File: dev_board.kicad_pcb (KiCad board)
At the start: 2 copper layers, 52 x 71.5 mm, 49 parts, among them J1 USB_B_Micro, J2 Conn_02x26_Odd_Even, J3 Conn_02x26_Odd_Even, J4 SM03B-SRSS-TB, SW1 SW_Push, SW2 SW_Push, U1 RP2350_80QFN, U2 NCP1117-3.3_SOT223, U3 W25Q128JVS, U4 DNF, Y1 ABM8-272-T3

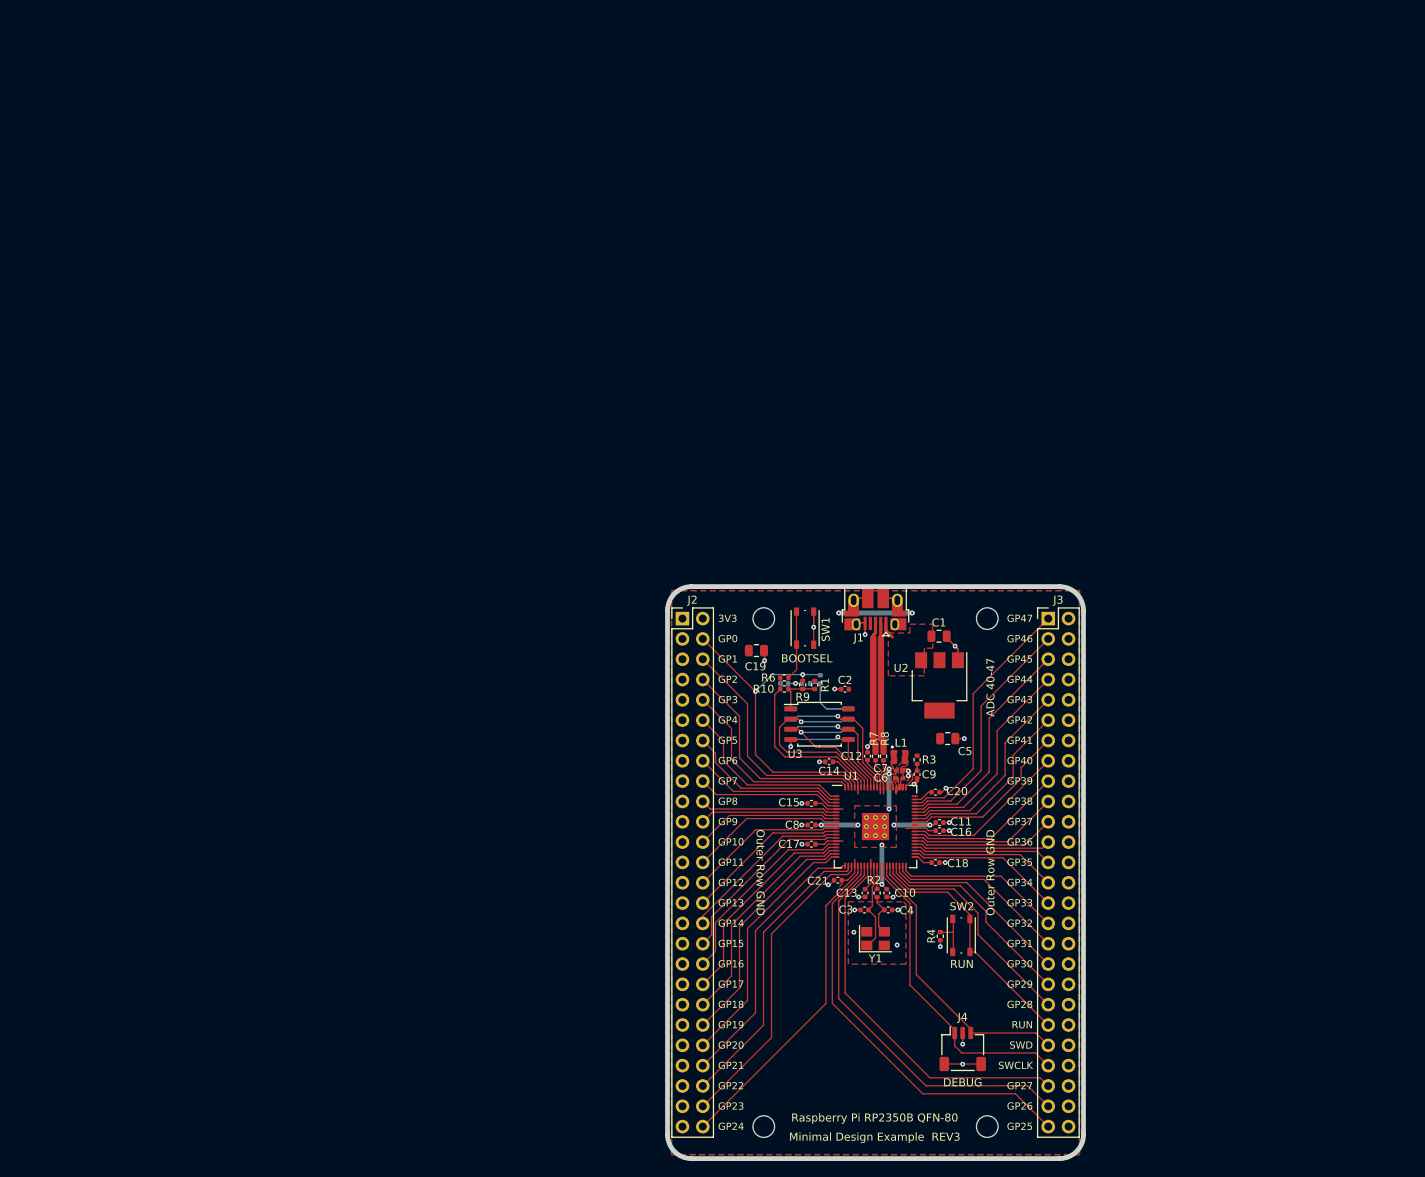
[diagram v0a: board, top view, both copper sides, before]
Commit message: more pcb chanegs, ADC fixes
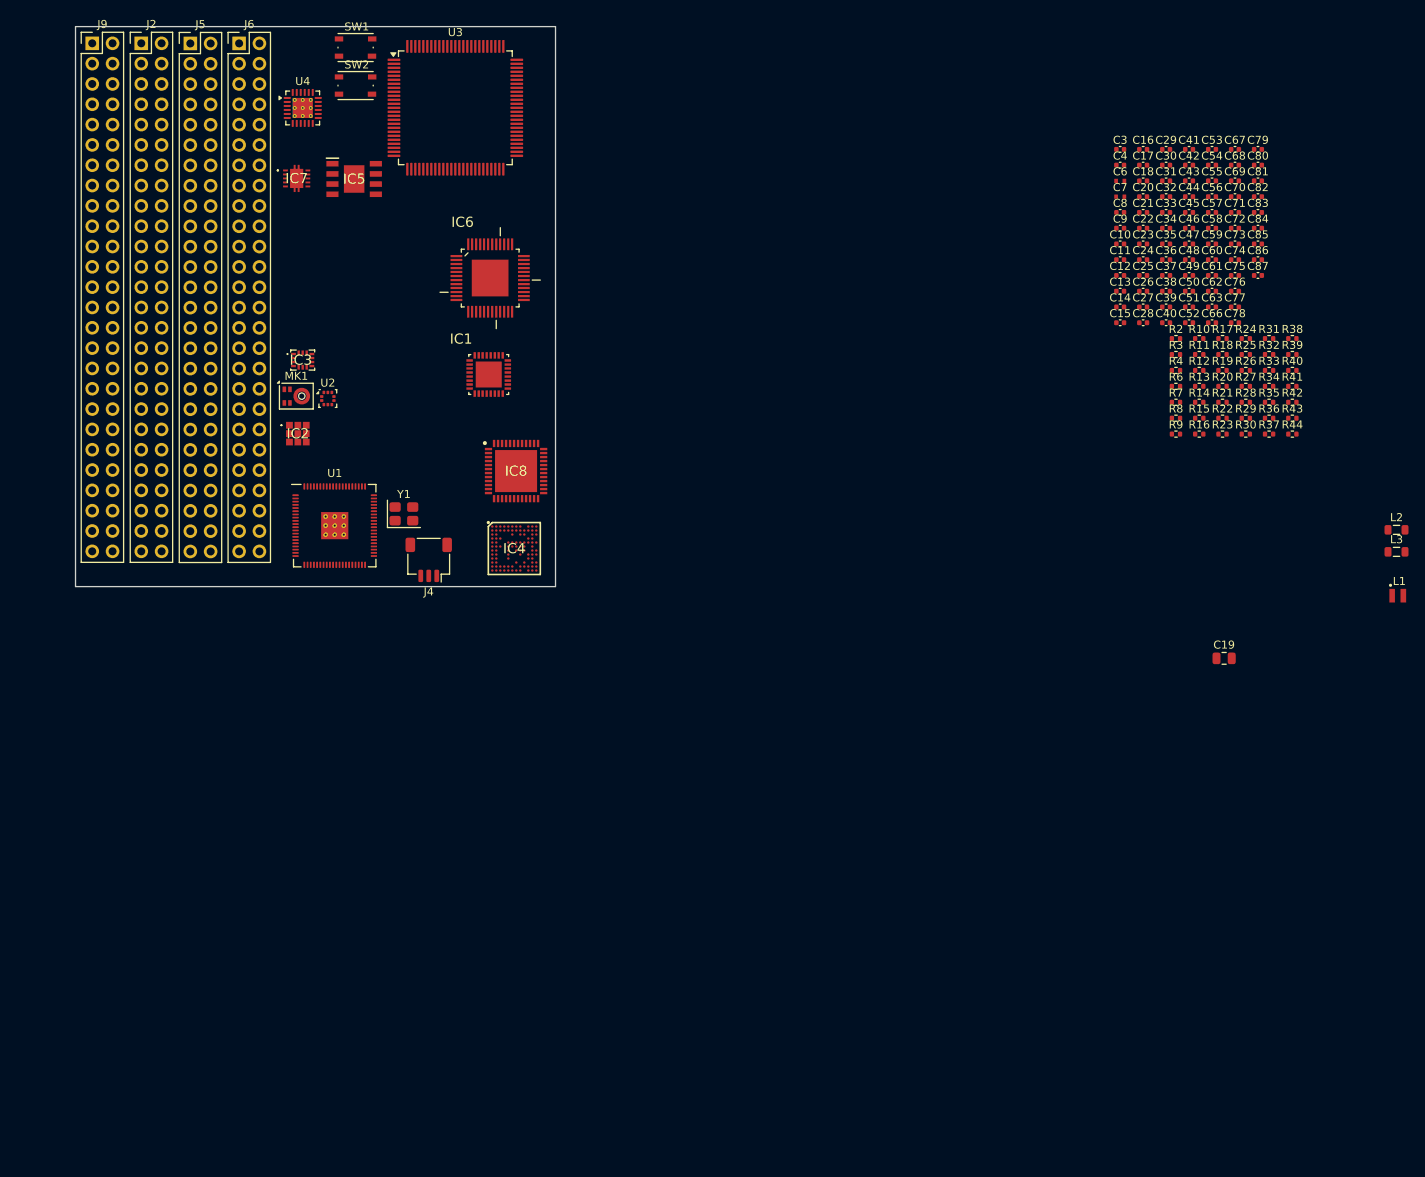
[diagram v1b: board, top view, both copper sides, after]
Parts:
- removed C1, C5: 10u, Capacitor_SMD:C_0805_2012Metric
- removed C2: 100n, Capacitor_SMD:C_0402_1005Metric
- removed H1, H2, H3, H4: MountingHole, MountingHole:MountingHole_2.7mm_M2.5
- removed J1: USB_B_Micro, Connector_USB:USB_Micro-B_Amphenol_10103594-0001LF_Horizontal
- removed J3: Conn_02x26_Odd_Even, Connector_PinHeader_2.54mm:PinHeader_2x26_P2.54mm_Vertical
- removed R1: DNF, Resistor_SMD:R_0402_1005Metric
- added C23: 100n, Capacitor_SMD:C_0402_1005Metric, F.Cu at (133.5, 27.2)
- added C24: 100n, Capacitor_SMD:C_0402_1005Metric, F.Cu at (133.5, 29.1)
- added C25: 10u, Capacitor_SMD:C_0402_1005Metric, F.Cu at (133.5, 31.1)
- added C26: 100n, Capacitor_SMD:C_0402_1005Metric, F.Cu at (133.5, 33.1)
- added C27: 100n, Capacitor_SMD:C_0402_1005Metric, F.Cu at (133.5, 35.0)
- added C28: 10u, Capacitor_SMD:C_0402_1005Metric, F.Cu at (133.5, 37.0)
- added C29: 1u, Capacitor_SMD:C_0402_1005Metric, F.Cu at (136.3, 15.3)
- added C30: 10u, Capacitor_SMD:C_0402_1005Metric, F.Cu at (136.3, 17.3)
- added C31: 10u, Capacitor_SMD:C_0402_1005Metric, F.Cu at (136.3, 19.3)
- added C32: 1u, Capacitor_SMD:C_0402_1005Metric, F.Cu at (136.3, 21.3)
- added C33: 100n, Capacitor_SMD:C_0402_1005Metric, F.Cu at (136.3, 23.2)
- added C34: 10u, Capacitor_SMD:C_0402_1005Metric, F.Cu at (136.3, 25.2)
- added C35: 10u, Capacitor_SMD:C_0402_1005Metric, F.Cu at (136.3, 27.2)
- added C36: 1u, Capacitor_SMD:C_0402_1005Metric, F.Cu at (136.3, 29.1)
- added C37: 1u, Capacitor_SMD:C_0402_1005Metric, F.Cu at (136.3, 31.1)
- added C38: 100n, Capacitor_SMD:C_0402_1005Metric, F.Cu at (136.3, 33.1)
- added C39: 10n, Capacitor_SMD:C_0402_1005Metric, F.Cu at (136.3, 35.0)
- added C40: 10n, Capacitor_SMD:C_0402_1005Metric, F.Cu at (136.3, 37.0)
- added C41: 100n, Capacitor_SMD:C_0402_1005Metric, F.Cu at (139.2, 15.3)
- added C42: 100n, Capacitor_SMD:C_0402_1005Metric, F.Cu at (139.2, 17.3)
- added C43: 100n, Capacitor_SMD:C_0402_1005Metric, F.Cu at (139.2, 19.3)
- added C44: 100n, Capacitor_SMD:C_0402_1005Metric, F.Cu at (139.2, 21.3)
- added C45: 100n, Capacitor_SMD:C_0402_1005Metric, F.Cu at (139.2, 23.2)
- added C46: 10u, Capacitor_SMD:C_0402_1005Metric, F.Cu at (139.2, 25.2)
- added C47: 2.2u, Capacitor_SMD:C_0402_1005Metric, F.Cu at (139.2, 27.2)
- added C48: 2.2u, Capacitor_SMD:C_0402_1005Metric, F.Cu at (139.2, 29.1)
- added C49: 100n, Capacitor_SMD:C_0402_1005Metric, F.Cu at (139.2, 31.1)
- added C50: 100n, Capacitor_SMD:C_0402_1005Metric, F.Cu at (139.2, 33.1)
- added C51: 100n, Capacitor_SMD:C_0402_1005Metric, F.Cu at (139.2, 35.0)
- added C52: 100n, Capacitor_SMD:C_0402_1005Metric, F.Cu at (139.2, 37.0)
- added C53: 10u, Capacitor_SMD:C_0402_1005Metric, F.Cu at (142.1, 15.3)
- added C54: 100n, Capacitor_SMD:C_0402_1005Metric, F.Cu at (142.1, 17.3)
- added C55: 100n, Capacitor_SMD:C_0402_1005Metric, F.Cu at (142.1, 19.3)
- added C56: 100n, Capacitor_SMD:C_0402_1005Metric, F.Cu at (142.1, 21.3)
- added C57: 100n, Capacitor_SMD:C_0402_1005Metric, F.Cu at (142.1, 23.2)
- added C58: 10u, Capacitor_SMD:C_0402_1005Metric, F.Cu at (142.1, 25.2)
- added C59: 100n, Capacitor_SMD:C_0402_1005Metric, F.Cu at (142.1, 27.2)
- added C60: 1u, Capacitor_SMD:C_0402_1005Metric, F.Cu at (142.1, 29.1)
- added C61: 100n, Capacitor_SMD:C_0402_1005Metric, F.Cu at (142.1, 31.1)
- added C62: 10u, Capacitor_SMD:C_0402_1005Metric, F.Cu at (142.1, 33.1)
- added C63: 100n, Capacitor_SMD:C_0402_1005Metric, F.Cu at (142.1, 35.0)
- added C66: 100n, Capacitor_SMD:C_0402_1005Metric, F.Cu at (142.1, 37.0)
- added C67: 100n, Capacitor_SMD:C_0402_1005Metric, F.Cu at (144.9, 15.3)
- added C68: 10u, Capacitor_SMD:C_0402_1005Metric, F.Cu at (144.9, 17.3)
- added C69: 2.2u, Capacitor_SMD:C_0402_1005Metric, F.Cu at (144.9, 19.3)
- added C70: 10u, Capacitor_SMD:C_0402_1005Metric, F.Cu at (144.9, 21.3)
- added C71: 2.2u, Capacitor_SMD:C_0402_1005Metric, F.Cu at (144.9, 23.2)
- added C72: 10u, Capacitor_SMD:C_0402_1005Metric, F.Cu at (144.9, 25.2)
- added C73: 2.2u, Capacitor_SMD:C_0402_1005Metric, F.Cu at (144.9, 27.2)
- added C74: 10u, Capacitor_SMD:C_0402_1005Metric, F.Cu at (144.9, 29.1)
- added C75: 100n, Capacitor_SMD:C_0402_1005Metric, F.Cu at (144.9, 31.1)
- added C76: 10u, Capacitor_SMD:C_0402_1005Metric, F.Cu at (144.9, 33.1)
- added C77: 100n, Capacitor_SMD:C_0402_1005Metric, F.Cu at (144.9, 35.0)
- added C78: 2.2u, Capacitor_SMD:C_0402_1005Metric, F.Cu at (144.9, 37.0)
- added C79: 2.2u, Capacitor_SMD:C_0402_1005Metric, F.Cu at (147.8, 15.3)
- added C80: 2.2u, Capacitor_SMD:C_0402_1005Metric, F.Cu at (147.8, 17.3)
- added C81: 10n, Capacitor_SMD:C_0402_1005Metric, F.Cu at (147.8, 19.3)
- added C82: 100n, Capacitor_SMD:C_0402_1005Metric, F.Cu at (147.8, 21.3)
- added C83: 10u, Capacitor_SMD:C_0402_1005Metric, F.Cu at (147.8, 23.2)
- added C84: 10u, Capacitor_SMD:C_0402_1005Metric, F.Cu at (147.8, 25.2)
- added C85: 100n, Capacitor_SMD:C_0402_1005Metric, F.Cu at (147.8, 27.2)
- added C86: 100n, Capacitor_SMD:C_0402_1005Metric, F.Cu at (147.8, 29.1)
- added C87: 100n, Capacitor_SMD:C_0402_1005Metric, F.Cu at (147.8, 31.1)
- added IC1: AD9609BCPZRL7-80, AD9609BCPZRL7-80:QFN50P500X500X100-33N, F.Cu at (51.6, 43.5)
- added IC2: ENS161-BLGT_LGA9_T&R_1k5, ENS161-BLGT_LGA9_T&R_1k5:ENS161BLGTLGA9TR1k5, F.Cu at (27.8, 50.9)
- added IC3: ICM-42670-P, ICM-42670-P:ICM42670P, F.Cu at (28.4, 41.7)
- added IC4: IWRL6432BDBAAMFR, IWRL6432BDBAAMFR:BGA102C50P12X12_645X645X97, F.Cu at (54.9, 65.2)
- added IC5: MP4541GN-Z, MP4541GN-Z:SOIC127P600X170-9N, F.Cu at (34.8, 19.1)
- added IC6: THS8136IPHPR, THS8136IPHPR:QFP50P900X900X120-49N, F.Cu at (51.8, 31.4)
- added IC7: TPS40304ADRCR, TPS40304ADRCR:TPS40304ADRCR, F.Cu at (27.6, 19.0)
- added IC8: XCC1352R1F3RGZR, XCC1352R1F3RGZR:QFN50P700X700X100-49N-D, F.Cu at (55.1, 55.6)
- added J5: STM32H7 GPIO/Fabric Breakout A, Connector_PinHeader_2.54mm:PinHeader_2x26_P2.54mm_Vertical, F.Cu at (14.3, 2.11)
- added J6: STM32H7 GPIO/Fabric Breakout B, Connector_PinHeader_2.54mm:PinHeader_2x26_P2.54mm_Vertical, F.Cu at (20.4, 2.10)
- added J9: HS/IWRL Fabric Breakout, Connector_PinHeader_2.54mm:PinHeader_2x26_P2.54mm_Vertical, F.Cu at (2.09, 2.09)
- added L2: 10uH, Inductor_SMD:L_0805_2012Metric, F.Cu at (165.1, 62.9)
- added L3: 4.7uH, Inductor_SMD:L_0805_2012Metric, F.Cu at (165.1, 65.7)
- added MK1: IM69D120, Sensor_Audio:Infineon_PG-LLGA-5-1, F.Cu at (27.6, 46.2)
- added R12: 10k, Resistor_SMD:R_0402_1005Metric, F.Cu at (140.5, 43.0)
- added R14: 330k, Resistor_SMD:R_0402_1005Metric, F.Cu at (140.5, 47.0)
- added R15: 100k, Resistor_SMD:R_0402_1005Metric, F.Cu at (140.5, 48.9)
- added R16: 100k, Resistor_SMD:R_0402_1005Metric, F.Cu at (140.5, 50.9)
- added R17: 10k, Resistor_SMD:R_0402_1005Metric, F.Cu at (143.4, 39.0)
- added R18: 10k, Resistor_SMD:R_0402_1005Metric, F.Cu at (143.4, 41.0)
- added R19: 10k, Resistor_SMD:R_0402_1005Metric, F.Cu at (143.4, 43.0)
- added R20: 0R, Resistor_SMD:R_0402_1005Metric, F.Cu at (143.4, 45.0)
- added R21: 0R, Resistor_SMD:R_0402_1005Metric, F.Cu at (143.4, 47.0)
- added R22: 10k, Resistor_SMD:R_0402_1005Metric, F.Cu at (143.4, 48.9)
- added R23: 10k, Resistor_SMD:R_0402_1005Metric, F.Cu at (143.4, 50.9)
- added R24: 12.1k, Resistor_SMD:R_0402_1005Metric, F.Cu at (146.3, 39.0)
- added R25: 2.2k, Resistor_SMD:R_0402_1005Metric, F.Cu at (146.3, 41.0)
- added R26: 10k, Resistor_SMD:R_0402_1005Metric, F.Cu at (146.3, 43.0)
- added R27: 10k, Resistor_SMD:R_0402_1005Metric, F.Cu at (146.3, 45.0)
- added R28: 10k, Resistor_SMD:R_0402_1005Metric, F.Cu at (146.3, 47.0)
- added R29: 10k, Resistor_SMD:R_0402_1005Metric, F.Cu at (146.3, 48.9)
- added R30: 0R, Resistor_SMD:R_0402_1005Metric, F.Cu at (146.3, 50.9)
- added R31: 3.8k, Resistor_SMD:R_0402_1005Metric, F.Cu at (149.2, 39.0)
- added R32: 75, Resistor_SMD:R_0402_1005Metric, F.Cu at (149.2, 41.0)
- added R33: 75, Resistor_SMD:R_0402_1005Metric, F.Cu at (149.2, 43.0)
- added R34: 75, Resistor_SMD:R_0402_1005Metric, F.Cu at (149.2, 45.0)
- added R35: 49.9, Resistor_SMD:R_0402_1005Metric, F.Cu at (149.2, 47.0)
- added R36: 49.9, Resistor_SMD:R_0402_1005Metric, F.Cu at (149.2, 48.9)
- added R37: 49.9, Resistor_SMD:R_0402_1005Metric, F.Cu at (149.2, 50.9)
- added R38: 49.9, Resistor_SMD:R_0402_1005Metric, F.Cu at (152.1, 39.0)
- added R39: 2.2k, Resistor_SMD:R_0402_1005Metric, F.Cu at (152.1, 41.0)
- added R40: 2.2k, Resistor_SMD:R_0402_1005Metric, F.Cu at (152.1, 43.0)
- added R41: 2.2k, Resistor_SMD:R_0402_1005Metric, F.Cu at (152.1, 45.0)
- added R42: 75, Resistor_SMD:R_0402_1005Metric, F.Cu at (152.1, 47.0)
- added R43: 75, Resistor_SMD:R_0402_1005Metric, F.Cu at (152.1, 48.9)
- added R44: 75, Resistor_SMD:R_0402_1005Metric, F.Cu at (152.1, 50.9)
- C22: value DNF -> 100n; moved to F.Cu
- R10: value 0 -> 4.7k
- R11, R13: value DNF -> 10k; moved to F.Cu
- R9: value DNF -> 4.7k
- U2: value NCP1117-3.3_SOT223 -> LPS22HH; footprint Package_TO_SOT_SMD:SOT-223-3_TabPin2 -> Package_LGA:ST_HLGA-10_2x2mm_P0.5mm_LayoutBorder3x2y
- U3: value W25Q128JVS -> STM32H750VBTx; footprint Package_SO:SOIC-8_5.23x5.23mm_P1.27mm -> Package_QFP:LQFP-100_14x14mm_P0.5mm
- U4: value DNF -> LAN8742A; footprint Package_SO:SOIC-8_5.23x5.23mm_P1.27mm -> Package_DFN_QFN:VQFN-24-1EP_4x4mm_P0.5mm_EP2.5x2.5mm_ThermalVias; moved to F.Cu
- moved SW2 130.5 mm to (35.0, 7.37), turned to 0 degrees
- moved U4 100.5 mm to (28.4, 10.2), turned to 0 degrees
- moved C3 100.3 mm to (130.6, 15.3), turned to 0 degrees
- moved J2 98.7 mm to (8.22, 2.09)
- moved C4 97.5 mm to (130.6, 17.3)
- moved C17 94.5 mm to (133.5, 17.3), turned to 0 degrees
- moved SW1 91.8 mm to (35.0, 2.62), turned to 0 degrees
- moved C21 91.8 mm to (133.5, 23.2), turned to 0 degrees
- moved J4 90.5 mm to (44.1, 66.7), turned to 180 degrees
- moved U3 89.5 mm to (47.5, 10.2)
- moved C18 89.1 mm to (133.5, 19.3)
- moved C16 88.9 mm to (133.5, 15.3)
- moved C10 86.2 mm to (130.6, 27.2), turned to 0 degrees
- moved C8 85.7 mm to (130.6, 23.2), turned to 0 degrees
- moved U2 84.5 mm to (31.5, 46.5), turned to 0 degrees
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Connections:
- J2 pad 1: GND -> /GPIO47_ADC7
- J2 pad 11: GND -> /GPIO42_ADC2
- J2 pad 13: GND -> /GPIO41_ADC1
- J2 pad 15: GND -> /GPIO40_ADC0
- J2 pad 17: GND -> /GPIO39
- J2 pad 19: GND -> /GPIO38
- J2 pad 21: GND -> /GPIO37
- J2 pad 23: GND -> /GPIO36
- J2 pad 25: GND -> /GPIO35
- J2 pad 27: GND -> /GPIO34
- J2 pad 29: GND -> /GPIO33
- J2 pad 3: GND -> /GPIO46_ADC6
- J2 pad 31: GND -> /GPIO32
- J2 pad 33: GND -> /GPIO31
- J2 pad 35: GND -> /GPIO30
- J2 pad 37: GND -> /GPIO29
- J2 pad 39: GND -> /GPIO28
- J2 pad 41: GND -> /RUN
- J2 pad 43: GND -> /SWD
- J2 pad 45: GND -> /SWCLK
- J2 pad 47: GND -> /GPIO27
- J2 pad 49: GND -> /GPIO26
- J2 pad 5: GND -> /GPIO45_ADC5
- J2 pad 51: GND -> /GPIO25
- J2 pad 7: GND -> /GPIO44_ADC4
- J2 pad 9: GND -> /GPIO43_ADC3
- R10 pad 1: /QSPI_SS -> +3V3
- R10 pad 2: /FLASH_SS -> /SENS_I2C_SDA
- R11 pad 1: /GPIO0 -> /ENS_ADDR
- R11 pad 2: /FLASH2_SS -> GND
- R13 pad 2: /FLASH2_SS -> /CC_RESET_N
- R9 pad 1: /GPIO0 -> +3V3
- R9 pad 2: /FLASH_SS -> /SENS_I2C_SCL
- U2 pad 1: GND -> +3V3
- U2 pad 2: +3V3 -> /SENS_I2C_SCL
- U2 pad 3: VBUS -> GND
- U3 pad 1: /FLASH_SS -> /ADC_D2
- U3 pad 2: /QSPI_SD1 -> /ADC_D3
- U3 pad 3: /QSPI_SD2 -> /ADC_D4
- U3 pad 4: GND -> /ADC_D5
- U3 pad 5: /QSPI_SD0 -> /ADC_D6
- U3 pad 6: /QSPI_SCLK -> +3V3
- U3 pad 7: /QSPI_SD3 -> /GPIO34
- U3 pad 8: +3V3 -> /GPIO35
- U4 pad 1: /FLASH2_SS -> +3V3
- U4 pad 2: /QSPI_SD1 -> /PHY_LED2_INTSEL
- U4 pad 3: /QSPI_SD2 -> /PHY_LED1_REGOFF
- U4 pad 4: GND -> /PHY_XTAL2
- U4 pad 5: /QSPI_SD0 -> /PHY_XTAL1
- U4 pad 6: /QSPI_SCLK -> /PHY_VDDCR
- U4 pad 7: /QSPI_SD3 -> /ETH_RXD1
- U4 pad 8: +3V3 -> /ETH_RXD0
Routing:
- net +3V3: track 52.9 -> 0.00 mm, vias 3 -> 0
- net /GPIO25: track 52.1 -> 0.00 mm
- net /GPIO26: track 49.7 -> 0.00 mm
- net /GPIO27: track 47.3 -> 0.00 mm
- net /GPIO0: track 41.5 -> 0.00 mm, vias 2 -> 0
- net /GPIO24: track 40.6 -> 0.00 mm
- net /GPIO23: track 39.0 -> 0.00 mm
- net /SWCLK: track 38.9 -> 0.00 mm
- net GND: track 38.8 -> 0.00 mm, vias 29 -> 0
- net /GPIO22: track 36.7 -> 0.00 mm
- net /SWD: track 35.6 -> 0.00 mm
- net /GPIO21: track 34.2 -> 0.00 mm
- net /GPIO47_ADC7: track 31.7 -> 0.00 mm
- net /GPIO20: track 31.7 -> 0.00 mm
- net /RUN: track 31.4 -> 0.00 mm
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- removed copper zone on F.Cu, net +1V1
- removed copper zone on F.Cu, net +3V3
- removed copper zone on F.Cu, net /VREG_LX
- removed copper zone on B.Cu, net GND
- removed copper zone on F.Cu, net GND
- removed copper zone on F.Cu, net VBUS
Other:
- board size 52 x 71.5 mm -> 60 x 70 mm
- rule pad_to_mask_clearance: 0.03 -> 0
- board text removed: "3V3"
- board text removed: "ADC 40-47"
- board text removed: "BOOTSEL"
- board text removed: "DEBUG"
- board text removed: "GP0"
- board text removed: "GP1"
- board text removed: "GP10"
- board text removed: "GP11"
- board text removed: "GP12"
- board text removed: "GP13"
- board text removed: "GP14"
- board text removed: "GP15"
- board text removed: "GP16"
- board text removed: "GP17"
- board text removed: "GP18"
- board text removed: "GP19"
- board text removed: "GP2"
- board text removed: "GP20"
- board text removed: "GP21"
- board text removed: "GP22"
- board text removed: "GP23"
- board text removed: "GP24"
- board text removed: "GP25"
- board text removed: "GP26"
- board text removed: "GP27"
- board text removed: "GP28"
- board text removed: "GP29"
- board text removed: "GP3"
- board text removed: "GP30"
- board text removed: "GP31"
- board text removed: "GP32"
- board text removed: "GP33"
- board text removed: "GP34"
- board text removed: "GP35"
- board text removed: "GP36"
- board text removed: "GP37"
- board text removed: "GP38"
- board text removed: "GP39"
- board text removed: "GP4"
- board text removed: "GP40"
- board text removed: "GP41"
- board text removed: "GP42"
- board text removed: "GP43"
- board text removed: "GP44"
- board text removed: "GP45"
- board text removed: "GP46"
- board text removed: "GP47"
- board text removed: "GP5"
- board text removed: "GP6"
- board text removed: "GP7"
- board text removed: "GP8"
- board text removed: "GP9"
- board text removed: "Minimal Design Example REV3"
- board text removed: "Outer Row GND"
- board text removed: "RUN"
- board text removed: "Raspberry Pi RP2350B QFN-80"
- board text removed: "SWCLK"
- board text removed: "SWD"

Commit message: more pcb chanegs, placements
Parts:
- added C88: 100n, Capacitor_SMD:C_0402_1005Metric, F.Cu at (11.9, 32.7)
- added C89: 1n, Capacitor_SMD:C_0402_1005Metric, F.Cu at (13.9, 32.7)
- added C90: 100n, Capacitor_SMD:C_0402_1005Metric, F.Cu at (27.9, 42.6)
- added C91: 22p, Capacitor_SMD:C_0402_1005Metric, F.Cu at (48.3, 29.7)
- added J10: RJ45 / 8P8C LED, Connector_RJ:RJ45_Amphenol_RJMG1BD3B8K1ANR, F.Cu at (86.7, 13.0)
- added J11: SMA_RF_LAUNCH, Connector_Coaxial:SMA_Amphenol_132134-10_Vertical, F.Cu at (4.50, 45.6)
- added J12: RP2350 USB PROGRAM, Connector_USB:USB_Micro-B_Amphenol_10103594-0001LF_Horizontal, F.Cu at (85.8, 47.2)
- added J13: STM32 USB DFU ALT, Connector_USB:USB_Micro-B_Amphenol_10103594-0001LF_Horizontal, F.Cu at (95.4, 47.2)
- added J14: CC1352 PROG BRIDGE USB, Connector_USB:USB_Micro-B_Amphenol_10103594-0001LF_Horizontal, F.Cu at (13.1, 47.2)
- added R45: 1k, Resistor_SMD:R_0402_1005Metric, F.Cu at (98.2, 33.4)
- added R46: 1k, Resistor_SMD:R_0402_1005Metric, F.Cu at (55.0, 29.1)
- added R47: 1k, Resistor_SMD:R_0402_1005Metric, F.Cu at (98.0, 19.5)
- added R48: 1k, Resistor_SMD:R_0402_1005Metric, F.Cu at (12.2, 29.7)
- added R49: 33, Resistor_SMD:R_0402_1005Metric, F.Cu at (14.2, 29.7)
- added R50: 33, Resistor_SMD:R_0402_1005Metric, F.Cu at (16.1, 29.7)
- added R51: 0R/DNP, Resistor_SMD:R_0402_1005Metric, F.Cu at (18.1, 29.7)
- added TP1: TestPoint, TestPoint:TestPoint_Pad_3.0x3.0mm, F.Cu at (44.7, 47.8)
- added TP2: TestPoint, TestPoint:TestPoint_Pad_3.0x3.0mm, F.Cu at (54.5, 47.8)
- added U5: PGA113, Package_SO:TSSOP-10_3x3mm_P0.5mm, F.Cu at (49.5, 41.1)
- added U6: MCP6D11T-E/MS, MCP6D11T:MCP6D11T-E_MSOP-8_3x3mm_P0.65mm, F.Cu at (49.6, 46.2)
- moved R28 145.1 mm to (2.21, 29.7), turned to 90 degrees
- moved R29 143.4 mm to (4.20, 29.7), turned to 90 degrees
- moved R30 141.7 mm to (6.19, 29.7), turned to 90 degrees
- moved R31 141.3 mm to (8.18, 29.7), turned to 90 degrees
- moved R32 139.5 mm to (10.2, 29.7), turned to 90 degrees
- moved L2 138.8 mm to (30.7, 28.6)
- moved L3 138.8 mm to (30.7, 31.4)
- moved C87 137.9 mm to (9.93, 32.7), turned to 90 degrees
- moved C76 135.0 mm to (9.93, 35.6), turned to 90 degrees
- moved C69 134.1 mm to (13.0, 43.6)
- moved C67 133.1 mm to (13.9, 38.5), turned to 90 degrees
- moved C77 133.0 mm to (11.9, 35.6), turned to 90 degrees
- moved C53 132.7 mm to (11.9, 41.3), turned to 90 degrees
- moved C63 132.2 mm to (9.93, 38.5), turned to 90 degrees
- moved R38 132.0 mm to (20.4, 29.5), turned to 90 degrees
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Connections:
- net Net-(U1-USB_DM) renamed /CC_SPI_MISO
- net Net-(U1-USB_DP) renamed /CC_SPI_CS_N
- IC2 pad 2: /SENS_I2C_SCL -> unconnected-(IC2-SCLK_/_SCL-Pad2)
- IC2 pad 3: /ENS_ADDR -> unconnected-(IC2-MISO_/_ADDR-Pad3)
- IC2 pad 4: +3V3 -> unconnected-(IC2-VDD-Pad4)
- IC2 pad 5: +3V3 -> unconnected-(IC2-VDDIO-Pad5)
- IC2 pad 7: +3V3 -> unconnected-(IC2-CSN-Pad7)
- IC2 pad 8: GND -> unconnected-(IC2-VSS_1-Pad8)
- IC2 pad 9: GND -> unconnected-(IC2-VSS_2-Pad9)
- IC3 pad 4: /GPIO7 -> unconnected-(IC3-INT1_/_INT-Pad4)
- IC3 pad 5: +3V3 -> unconnected-(IC3-VDDIO-Pad5)
- IC3 pad 6: GND -> unconnected-(IC3-GND-Pad6)
- IC3 pad 7: /IMU_FSYNC -> unconnected-(IC3-FSYNC-Pad7)
- IC3 pad 9: /GPIO8 -> unconnected-(IC3-INT2-Pad9)
- IC8 pad 1: /CC_RF_P_2G4 -> unconnected-(IC8-RF_P_2_4GHZ-Pad1)
- IC8 pad 2: /CC_RF_N_2G4 -> unconnected-(IC8-RF_N_2_4GHZ-Pad2)
- IC8 pad 3: /CC_RF_P_SUBG -> unconnected-(IC8-RF_P_SUB_1GHZ-Pad3)
- IC8 pad 4: /CC_RF_N_SUBG -> unconnected-(IC8-RF_N_SUB_1GHZ-Pad4)
- IC8 pad 6: /CC_X32K_Q1 -> unconnected-(IC8-X32K_Q1-Pad6)
- IC8 pad 7: /CC_X32K_Q2 -> unconnected-(IC8-X32K_Q2-Pad7)
- MK1 pad 1: /GPIO3 -> GND
- MK1 pad 2: +3V3 -> GND
- MK1 pad 4: GND -> /GPIO3
- MK1 pad 5: GND -> +3V3
- U2 pad 1: +3V3 -> unconnected-(U2-Vdd_IO-Pad1)
- U2 pad 10: +3V3 -> unconnected-(U2-VDD-Pad10)
- U2 pad 2: /SENS_I2C_SCL -> unconnected-(U2-SCL-Pad2)
- U2 pad 3: GND -> +3V3
- U2 pad 4: /SENS_I2C_SDA -> unconnected-(U2-SDA-Pad4)
- U2 pad 5: /LPS_SA0 -> /GPIO9
- U2 pad 7: /GPIO9 -> /LPS_SA0
- U2 pad 8: GND -> +3V3
- U2 pad 9: GND -> +3V3
- U3 pad 12: /GPIO37 -> /STM_VCAP_A
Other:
- board size 60 x 70 mm -> 100 x 50 mm
- copper layers 2 -> 4

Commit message: more fixes
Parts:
- removed R20, R21: 0R, Resistor_SMD:R_0402_1005Metric
- added C92: 100n, Capacitor_SMD:C_0402_1005Metric, F.Cu at (85.4, 35.4)
- added C93: 100n, Capacitor_SMD:C_0402_1005Metric, F.Cu at (85.4, 33.4)
- added C94: 100n, Capacitor_SMD:C_0402_1005Metric, F.Cu at (85.4, 31.4)
- added J15: IWRL USB PROGRAM, Connector_USB:USB_Micro-B_Amphenol_10103594-0001LF_Horizontal, F.Cu at (97.2, 38.3)
- added U7: FT232RNL-TUBE, Package_SO:SSOP-28_5.3x10.2mm_P0.65mm, F.Cu at (40.4, 37.8)
- moved R47 45.1 mm to (53.9, 29.1), turned to -90 degrees
- moved C21 38.8 mm to (74.6, 47.2)
- moved C22 38.8 mm to (74.6, 49.2)
- moved C33 38.8 mm to (77.5, 49.2)
- moved C57 38.8 mm to (80.4, 47.2)
- moved C59 38.8 mm to (80.4, 49.2)
- moved C60 38.8 mm to (77.5, 47.2)
- moved C74 32.4 mm to (69.8, 49.1)
- moved C20 32.4 mm to (66.9, 49.1)
- moved C30 32.4 mm to (69.8, 47.2)
- moved C18 32.4 mm to (66.9, 47.2)
- moved C41 32.4 mm to (72.7, 47.2)
- moved C56 32.4 mm to (72.7, 49.1)
- moved C29 26.9 mm to (61.8, 48.8)
- moved C51 26.9 mm to (64.7, 48.8)
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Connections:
- net /CC_SPI_CS_N renamed Net-(U1-USB_DP)
- net /CC_SPI_MISO renamed Net-(U1-USB_DM)
- C89 pad 2: +3V3 -> Net-(U6-IN-)
- C90 pad 2: +3V3 -> Net-(U6-OUT+)
- IC2 pad 2: unconnected-(IC2-SCLK_/_SCL-Pad2) -> /SENS_I2C_SCL
- IC2 pad 3: unconnected-(IC2-MISO_/_ADDR-Pad3) -> /ENS_ADDR
- IC2 pad 4: unconnected-(IC2-VDD-Pad4) -> +3V3
- IC2 pad 5: unconnected-(IC2-VDDIO-Pad5) -> +3V3
- IC2 pad 6: /GPIO6 -> unconnected-(IC2-INTN-Pad6)
- IC2 pad 7: unconnected-(IC2-CSN-Pad7) -> /GPIO6
- IC2 pad 8: unconnected-(IC2-VSS_1-Pad8) -> GND
- IC2 pad 9: unconnected-(IC2-VSS_2-Pad9) -> GND
- IC3 pad 4: unconnected-(IC3-INT1_/_INT-Pad4) -> /GPIO7
- IC3 pad 5: unconnected-(IC3-VDDIO-Pad5) -> +3V3
- IC3 pad 6: unconnected-(IC3-GND-Pad6) -> GND
- IC3 pad 7: unconnected-(IC3-FSYNC-Pad7) -> +3V3
- IC8 pad 1: unconnected-(IC8-RF_P_2_4GHZ-Pad1) -> /CC_RF_P_2G4
- IC8 pad 2: unconnected-(IC8-RF_N_2_4GHZ-Pad2) -> /CC_RF_N_2G4
- IC8 pad 3: unconnected-(IC8-RF_P_SUB_1GHZ-Pad3) -> /CC_RF_P_SUBG
- IC8 pad 4: unconnected-(IC8-RF_N_SUB_1GHZ-Pad4) -> /CC_RF_N_SUBG
- IC8 pad 6: unconnected-(IC8-X32K_Q1-Pad6) -> /CC_X32K_Q1
- IC8 pad 7: unconnected-(IC8-X32K_Q2-Pad7) -> /CC_X32K_Q2
- J12 pad 1: unconnected-(J12-VBUS-Pad1) -> /VIN_RAW
- J12 pad 4: /VIN_RAW -> unconnected-(J12-ID-Pad4)
- J14 pad 1: unconnected-(J14-VBUS-Pad1) -> /VIN_RAW
- J2 pad 33: /GPIO31 -> /CC_DIO_10
- J2 pad 35: /GPIO30 -> /CC_DIO_9
- J2 pad 37: /GPIO29 -> /CC_DIO_8
- J2 pad 39: /GPIO28 -> /CC_DIO_7
- J2 pad 47: /GPIO27 -> /CC_DIO_6
- MK1 pad 1: GND -> /GPIO4
- R46 pad 2: +3V3 -> Net-(U6-IN-)
- R47 pad 1: +3V3 -> Net-(U6-IN-)
- R47 pad 2: +3V3 -> Net-(U6-OUT+)
- R50 pad 1: +3V3 -> Net-(U6-OUT+)
- U1 pad 28: /GPIO27 -> /CC_DIO_6
- U1 pad 36: /GPIO28 -> /CC_DIO_7
- U1 pad 37: /GPIO29 -> /CC_DIO_8
- U1 pad 38: /GPIO30 -> /CC_DIO_9
- U1 pad 39: /GPIO31 -> /CC_DIO_10
- U2 pad 1: unconnected-(U2-Vdd_IO-Pad1) -> +3V3
- U2 pad 10: unconnected-(U2-VDD-Pad10) -> +3V3
- U2 pad 2: unconnected-(U2-SCL-Pad2) -> /SENS_I2C_SCL
- U2 pad 3: +3V3 -> GND
- U2 pad 4: unconnected-(U2-SDA-Pad4) -> /SENS_I2C_SDA
- U2 pad 5: /GPIO9 -> /LPS_SA0
- U2 pad 7: /LPS_SA0 -> /GPIO9
- U2 pad 8: +3V3 -> GND
- U2 pad 9: +3V3 -> GND
- U6 pad 1: +3V3 -> Net-(U6-IN-)
- U6 pad 4: +3V3 -> Net-(U6-OUT+)

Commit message: more fixes
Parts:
- added IC10: MP4541GN-Z, MP4541GN-Z:SOIC127P600X170-9N, F.Cu at (79.0, 23.2)
- added IC9: TPS40304ADRCR, TPS40304ADRCR:TPS40304ADRCR, F.Cu at (78.8, 15.8)
- added TP3: TestPoint, TestPoint:TestPoint_Pad_3.0x3.0mm, F.Cu at (58.8, 47.9)
- added TP4: TestPoint, TestPoint:TestPoint_Pad_3.0x3.0mm, F.Cu at (63.8, 47.9)
- added TP5: TestPoint, TestPoint:TestPoint_Pad_3.0x3.0mm, F.Cu at (68.9, 47.9)
- moved C11 74.1 mm to (0.95, 29.6)
- moved C30 50.6 mm to (19.6, 41.1)
- moved C74 50.6 mm to (19.6, 43.1)
- moved C18 50.6 mm to (16.7, 41.1)
- moved C20 50.6 mm to (16.7, 43.1)
- moved C29 43.7 mm to (18.4, 44.0)
- moved C51 43.7 mm to (21.2, 44.0)
- moved C17 38.0 mm to (25.0, 31.6), turned to 180 degrees
- moved C63 37.8 mm to (46.8, 29.9)
- moved C56 34.8 mm to (44.6, 28.6)
- moved C57 34.5 mm to (50.4, 30.0), turned to 90 degrees
- moved C59 33.9 mm to (52.4, 30.0), turned to 90 degrees
- moved C60 28.5 mm to (54.3, 30.7)
- moved C62 24.8 mm to (51.5, 28.9), turned to 90 degrees
- moved C10 19.9 mm to (91.1, 42.5), turned to 0 degrees
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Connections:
- J9 pad 42: +3V3 -> GND
- J9 pad 48: +3V3 -> GND

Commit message: more fixes
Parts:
- moved U6 5.46 mm to (49.4, 40.8)
- moved U5 3.31 mm to (49.7, 44.4), turned to 180 degrees
- moved TP2 0.26 mm to (54.7, 47.9)
- moved J4 0.19 mm to (26.0, 46.7)
- moved J14 0.13 mm to (13.0, 47.2)
- turned IC6 to 180 degrees
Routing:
- net /VGA_G: track 0.00 -> 12.9 mm
- net /SCOPE_IN: track 0.00 -> 8.73 mm
- net /SCOPE_AUX_IN: track 0.00 -> 5.04 mm
- net /VGA_B: track 0.00 -> 5.02 mm
- net /VGA_R: track 0.00 -> 3.26 mm

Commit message: something
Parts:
- J13: value STM32 USB DFU ALT -> DNP / not used
- J14: value CC1352 PROG BRIDGE USB -> DNP / not used
- moved SW2 35.9 mm to (26.8, 34.3)
- moved IC3 35.2 mm to (62.8, 32.2)
- moved C17 7.30 mm to (31.3, 35.5)
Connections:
- J2 pad 43: /SWD -> +1V1
- J2 pad 45: /SWCLK -> /RP_SWCLK
- J4 pad 1: /SWCLK -> /RP_SWCLK
- J4 pad 3: /SWD -> +1V1
- L1 pad 2: /VREG_LX -> /RP_SWCLK
- U1 pad 33: /SWCLK -> /RP_SWCLK
- U1 pad 34: /SWD -> /VREG_FB
- U1 pad 63: /VREG_LX -> /RP_SWCLK
